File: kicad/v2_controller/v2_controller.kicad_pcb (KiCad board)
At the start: 2 copper layers, 100 x 116 mm, 131 parts, among them J1 Conn_02x10_Odd_Even, J2 Conn_02x10_Odd_Even, J3 USB_C_Receptacle_USB2.0, J4 USB_C_Receptacle_USB2.0, J5 Conn_02x04_Odd_Even, Q1 S8050, Q2 S8050, SW18 Boot, SW19 Reset, U1 ESP32-S3-WROOM-1-N16R8, U2 SSD1306_I2C, U3 74AHCT1G125, U4 AMS1117-3.3, U5 USBLC6-2P6, U6 USBLC6-2P6, U7 CP2102N-Axx-xQFN24

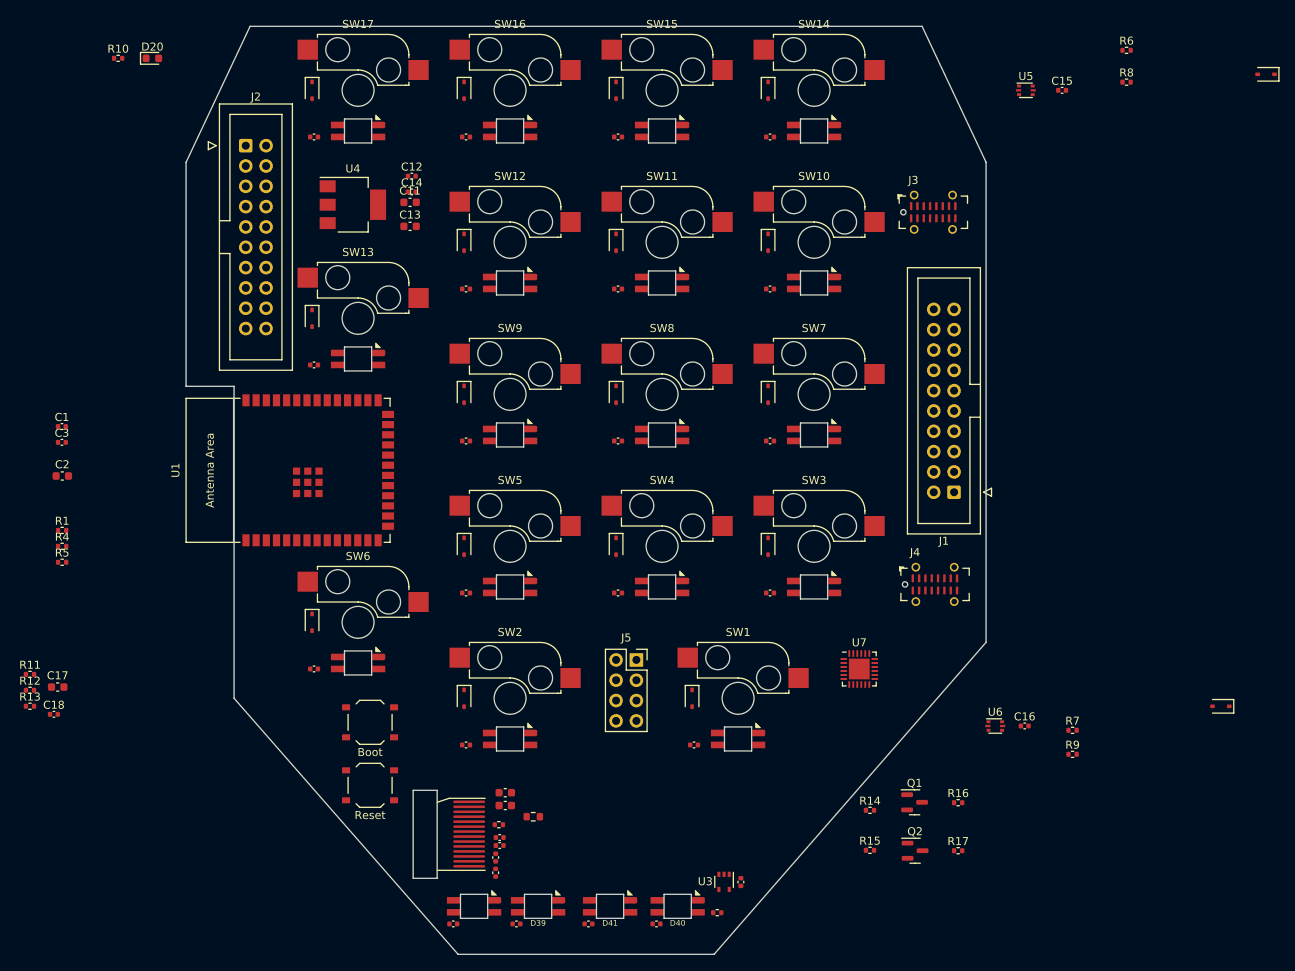
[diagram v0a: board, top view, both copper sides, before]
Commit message: [kicad] finish initial component placement
This will probably need to be tweaked further once I begin routing,
but is a start for now.
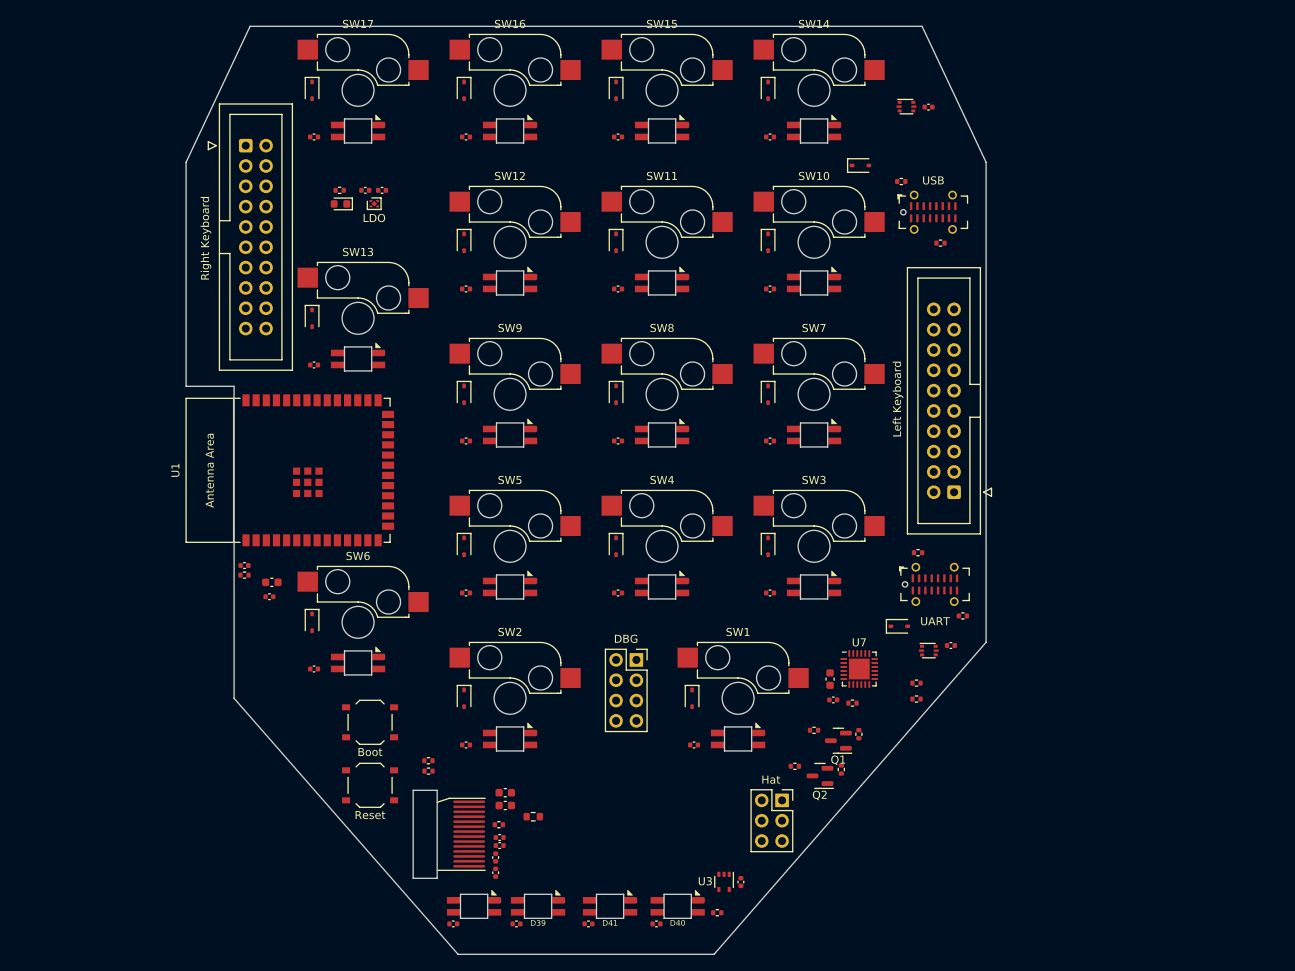
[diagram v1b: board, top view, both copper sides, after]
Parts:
- removed C13: 10uF, Capacitor_SMD:C_0603_1608Metric
- removed C14: 100nF, Capacitor_SMD:C_0402_1005Metric
- added J6: Conn_02x03_Odd_Even, Connector_PinSocket_2.54mm:PinSocket_2x03_P2.54mm_Vertical, F.Cu at (114.5, 136.8)
- C11: value 10uF -> 1uF; footprint Capacitor_SMD:C_0603_1608Metric -> Capacitor_SMD:C_0402_1005Metric
- C12: value 100nF -> 1uF
- U4: value AMS1117-3.3 -> NCP167BMX330TBG; footprint Package_TO_SOT_SMD:SOT-223-3_TabPin2 -> Package_DFN_QFN:OnSemi_XDFN4-1EP_1.0x1.0mm_EP0.52x0.52mm
- moved R13 110.8 mm to (131.3, 122.1)
- moved R14 110.8 mm to (131.3, 124.1)
- moved R15 102.8 mm to (123.3, 124.6), turned to 180 degrees
- moved C18 97.4 mm to (120.9, 124.2)
- moved C17 96.6 mm to (120.5, 121.6), turned to -90 degrees
- moved R2 53.0 mm to (70.3, 131.8)
- moved R3 52.7 mm to (70.3, 133.1)
- moved D18 52.0 mm to (124.3, 57.4), turned to 0 degrees
- moved D19 41.4 mm to (129.2, 115.0), turned to 0 degrees
- moved R8 32.6 mm to (129.4, 59.4)
- moved C3 32.3 mm to (50.4, 111.3)
- moved R12 32.2 mm to (59.2, 60.5)
- moved R9 30.8 mm to (134.3, 67.1)
- moved D20 29.7 mm to (59.3, 62.2), turned to 180 degrees
- moved R10 29.4 mm to (131.5, 105.8), turned to 180 degrees
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- renumbered J3 to J1, J4 to J2, J1 to J3, J2 to J4, R7 to R10, R9 to R11, R10 to R12, R11 to R13, R12 to R14, R13 to R15, R18 to R16, R2 to R17, R3 to R18, R4 to R2, R5 to R3, R14 to R4, R15 to R5, R16 to R6, R17 to R7, R6 to R8, R8 to R9
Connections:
- net /USB/USB1_VBUS renamed /USB/USB_VBUS
- C12 pad 1: +5V -> +3.3V
- C16 pad 1: /USB/USB2_VBUS -> /USB/UART_USB_VBUS
- D19 pad 2: /USB/USB2_VBUS -> /USB/UART_USB_VBUS
- J2 pad A4: /USB/USB2_VBUS -> /USB/UART_USB_VBUS
- J2 pad A9: /USB/USB2_VBUS -> /USB/UART_USB_VBUS
- J2 pad B4: /USB/USB2_VBUS -> /USB/UART_USB_VBUS
- J2 pad B9: /USB/USB2_VBUS -> /USB/UART_USB_VBUS
- R13 pad 1: +5V -> /USB/UART_USB_VBUS
- U1 pad 25: unconnected-(U1-GPIO48/SPICLK_N-Pad25) -> /ESP32/COL10
- U4 pad 1: GND -> +3.3V
- U4 pad 2: +3.3V -> GND
- U6 pad 5: /USB/USB2_VBUS -> /USB/UART_USB_VBUS

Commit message: [kicad] move the main USB receptacle closer to the ESP32
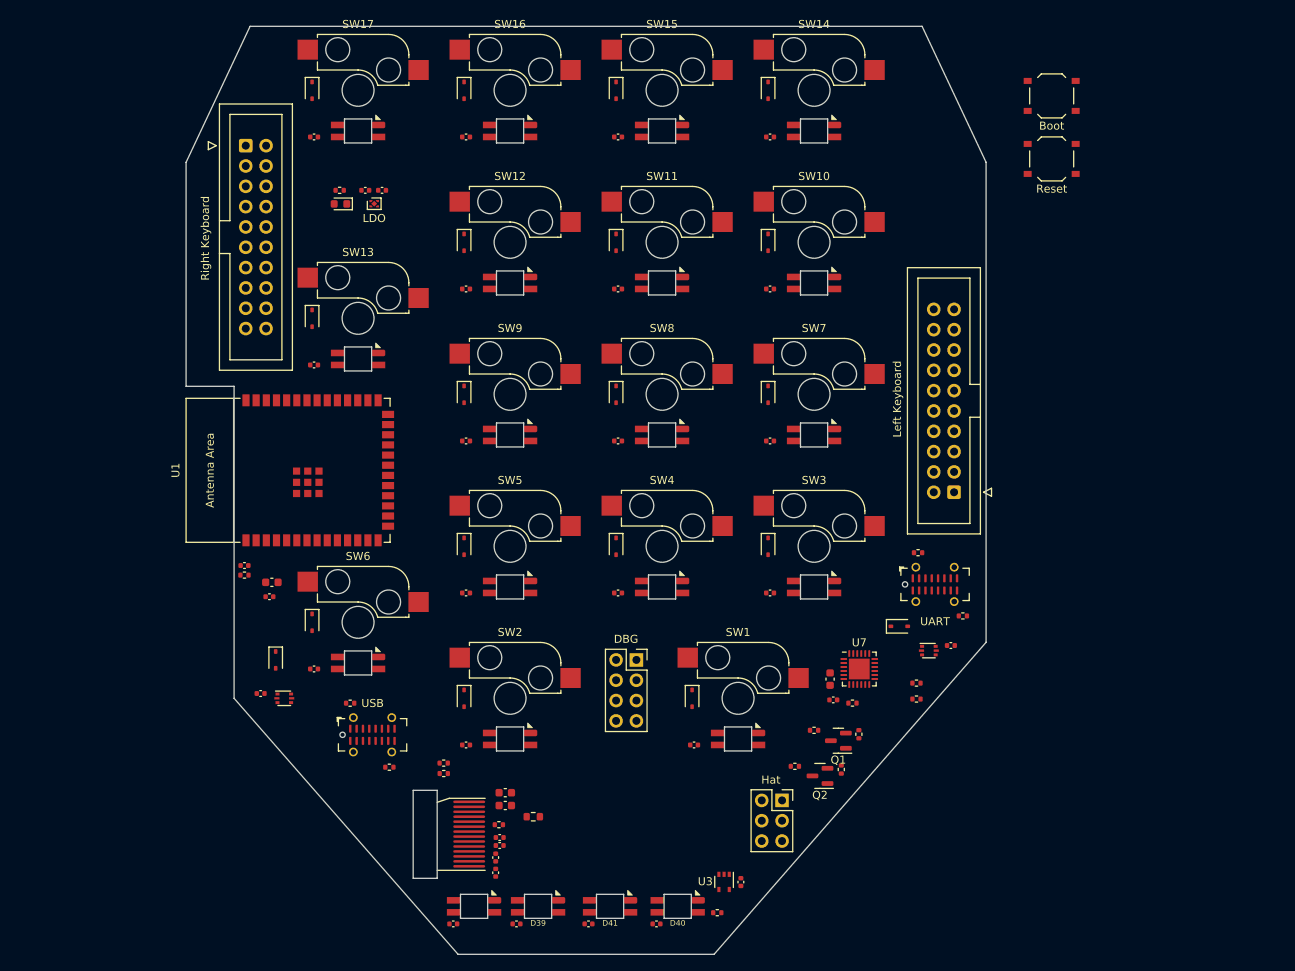
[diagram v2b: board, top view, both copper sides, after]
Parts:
- moved SW18 115.7 mm to (148.2, 48.7)
- moved SW19 115.7 mm to (148.2, 56.6)
- moved C15 111.1 mm to (49.3, 123.4)
- moved U5 107.3 mm to (52.3, 124.0)
- moved J1 95.8 mm to (63.3, 128.6)
- moved D18 95.7 mm to (51.2, 119.2), turned to -90 degrees
- moved R9 95.1 mm to (65.4, 132.6)
- moved R8 94.9 mm to (60.5, 124.6), turned to 180 degrees
- moved R3 1.93 mm to (72.2, 133.4)
- moved R2 1.93 mm to (72.2, 132.1)
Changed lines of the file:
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@@
   )
   (footprint "Resistor_SMD:R_0402_1005Metric" (layer "F.Cu")
-    (at 129.4 59.4)
+    (at 60.51 124.61 180)
     (descr "Resistor SMD 0402 (1005 Metric), square (rectangular) end terminal, IPC_7351 nominal, (Body size source: IPC-SM-782 page 72, https://www.pcb-3d.com/wordpress/wp-content/uploads/ipc-sm-782a_amendment_1_and_2.pdf), generated with kicad-footprint-generator")
     (tags "resistor")
@@
     (fp_line (start 0.525 0.27) (end -0.525 0.27)
       (stroke (width 0.1) (type solid)) (layer "F.Fab"))
-    (pad "1" smd roundrect (at -0.51 0) (size 0.54 0.64) (layers "F.Cu" "F.Paste" "F.Mask") (roundrect_rratio 0.25)
+    (pad "1" smd roundrect (at -0.51 0 180) (size 0.54 0.64) (layers "F.Cu" "F.Paste" "F.Mask") (roundrect_rratio 0.25)
       (net 67 "Net-(J1-CC1)") (pintype "passive"))
-    (pad "2" smd roundrect (at 0.51 0) (size 0.54 0.64) (layers "F.Cu" "F.Paste" "F.Mask") (roundrect_rratio 0.25)
+    (pad "2" smd roundrect (at 0.51 0 180) (size 0.54 0.64) (layers "F.Cu" "F.Paste" "F.Mask") (roundrect_rratio 0.25)
       (net 1 "GND") (pintype "passive"))
     (model "${KICAD6_3DMODEL_DIR}/Resistor_SMD.3dshapes/R_0402_1005Metric.wrl"
@@
   )
   (footprint "Connector_USB:USB_C_Receptacle_G-Switch_GT-USB-7051x" (layer "F.Cu")
-    (at 133.41 63.24)
+    (at 63.31 128.56)
     (descr "USB Type C, vertical, SMT, https://datasheet.lcsc.com/lcsc/2108072030_G-Switch-GT-USB-7051A_C2843970.pdf")
     (tags "USB C Type-C Receptacle SMD GT-USB-7051A GT-USB-7051B")
@@
       (polygon
         (pts
-          (xy 134.21 61.44)
-          (xy 132.61 61.44)
-          (xy 132.61 60.74)
-          (xy 134.21 60.74)
+          (xy 64.11 126.76)
+          (xy 62.51 126.76)
+          (xy 62.51 126.06)
+          (xy 64.11 126.06)
         )
       )
@@
       (polygon
         (pts
-          (xy 134.21 65.74)
-          (xy 132.61 65.74)
-          (xy 132.61 65.04)
-          (xy 134.21 65.04)
+          (xy 64.11 131.06)
+          (xy 62.51 131.06)
+          (xy 62.51 130.36)
+          (xy 64.11 130.36)
         )
       )
@@
   )
   (footprint "Resistor_SMD:R_0402_1005Metric" (layer "F.Cu")
-    (at 70.3 133.1)
+    (at 72.21 133.4)
     (descr "Resistor SMD 0402 (1005 Metric), square (rectangular) end terminal, IPC_7351 nominal, (Body size source: IPC-SM-782 page 72, https://www.pcb-3d.com/wordpress/wp-content/uploads/ipc-sm-782a_amendment_1_and_2.pdf), generated with kicad-footprint-generator")
     (tags "resistor")
@@
   )
   (footprint "Resistor_SMD:R_0402_1005Metric" (layer "F.Cu")
-    (at 134.3 67.1)
+    (at 65.41 132.61)
     (descr "Resistor SMD 0402 (1005 Metric), square (rectangular) end terminal, IPC_7351 nominal, (Body size source: IPC-SM-782 page 72, https://www.pcb-3d.com/wordpress/wp-content/uploads/ipc-sm-782a_amendment_1_and_2.pdf), generated with kicad-footprint-generator")
     (tags "resistor")
@@
   )
   (footprint "Resistor_SMD:R_0402_1005Metric" (layer "F.Cu")
-    (at 70.29 131.8)
+    (at 72.2 132.1)
     (descr "Resistor SMD 0402 (1005 Metric), square (rectangular) end terminal, IPC_7351 nominal, (Body size source: IPC-SM-782 page 72, https://www.pcb-3d.com/wordpress/wp-content/uploads/ipc-sm-782a_amendment_1_and_2.pdf), generated with kicad-footprint-generator")
     (tags "resistor")
@@
   )
   (footprint "Capacitor_SMD:C_0402_1005Metric" (layer "F.Cu")
-    (at 132.8 50.1)
+    (at 49.32 123.4)
     (descr "Capacitor SMD 0402 (1005 Metric), square (rectangular) end terminal, IPC_7351 nominal, (Body size source: IPC-SM-782 page 76, https://www.pcb-3d.com/wordpress/wp-content/uploads/ipc-sm-782a_amendment_1_and_2.pdf), generated with kicad-footprint-generator")
     (tags "capacitor")
@@
   )
   (footprint "Button_Switch_SMD:SW_Push_1P1T_XKB_TS-1187A" (layer "F.Cu")
-    (at 63 134.875)
+    (at 148.2 56.575)
     (descr "SMD Tactile Switch, http://www.helloxkb.com/public/images/pdf/TS-1187A-X-X-X.pdf")
     (tags "SPST Tactile Switch")
@@
   )
   (footprint "Button_Switch_SMD:SW_Push_1P1T_XKB_TS-1187A" (layer "F.Cu")
-    (at 63 127)
+    (at 148.2 48.7)
     (descr "SMD Tactile Switch, http://www.helloxkb.com/public/images/pdf/TS-1187A-X-X-X.pdf")
     (tags "SPST Tactile Switch")
@@
   )
   (footprint "Package_TO_SOT_SMD:SOT-666" (layer "F.Cu")
-    (at 130.05 50.0375)
+    (at 52.275 124)
     (descr "SOT666")
     (tags "SOT-666")
@@
   )
   (footprint "Diode_SMD:D_SOD-323" (layer "F.Cu")
-    (at 124.3 57.4)
+    (at 51.2 119.2 -90)
     (descr "SOD-323")
     (tags "SOD-323")
@@
     (property "ki_keywords" "diode Schottky")
     (attr smd)
-    (fp_text reference "D18" (at 0 -1.85) (layer "F.SilkS") hide
+    (fp_text reference "D18" (at 0 -1.85 90) (layer "F.SilkS") hide
         (effects (font (size 1 1) (thickness 0.15)))
     )
-    (fp_text value "1N5819WS" (at 0.1 1.9) (layer "F.Fab")
+    (fp_text value "1N5819WS" (at 0.1 1.9 90) (layer "F.Fab")
         (effects (font (size 1 1) (thickness 0.15)))
     )
-    (fp_text user "${REFERENCE}" (at 0 -1.85) (layer "F.Fab")
+    (fp_text user "${REFERENCE}" (at 0 -1.85 90) (layer "F.Fab")
         (effects (font (size 1 1) (thickness 0.15)))
     )
@@
     (fp_line (start 0.9 0.7) (end -0.9 0.7)
       (stroke (width 0.1) (type solid)) (layer "F.Fab"))
-    (pad "1" smd roundrect (at -1.05 0) (size 0.6 0.45) (layers "F.Cu" "F.Paste" "F.Mask") (roundrect_rratio 0.25)
+    (pad "1" smd roundrect (at -1.05 0 270) (size 0.6 0.45) (layers "F.Cu" "F.Paste" "F.Mask") (roundrect_rratio 0.25)
       (net 9 "+5V") (pinfunction "K") (pintype "passive"))
-    (pad "2" smd roundrect (at 1.05 0) (size 0.6 0.45) (layers "F.Cu" "F.Paste" "F.Mask") (roundrect_rratio 0.25)
+    (pad "2" smd roundrect (at 1.05 0 270) (size 0.6 0.45) (layers "F.Cu" "F.Paste" "F.Mask") (roundrect_rratio 0.25)
       (net 129 "/USB/USB_VBUS") (pinfunction "A") (pintype "passive"))
     (model "${KICAD6_3DMODEL_DIR}/Diode_SMD.3dshapes/D_SOD-323.wrl"

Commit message: [kicad] tweak the pcb layout with a slightly larger board
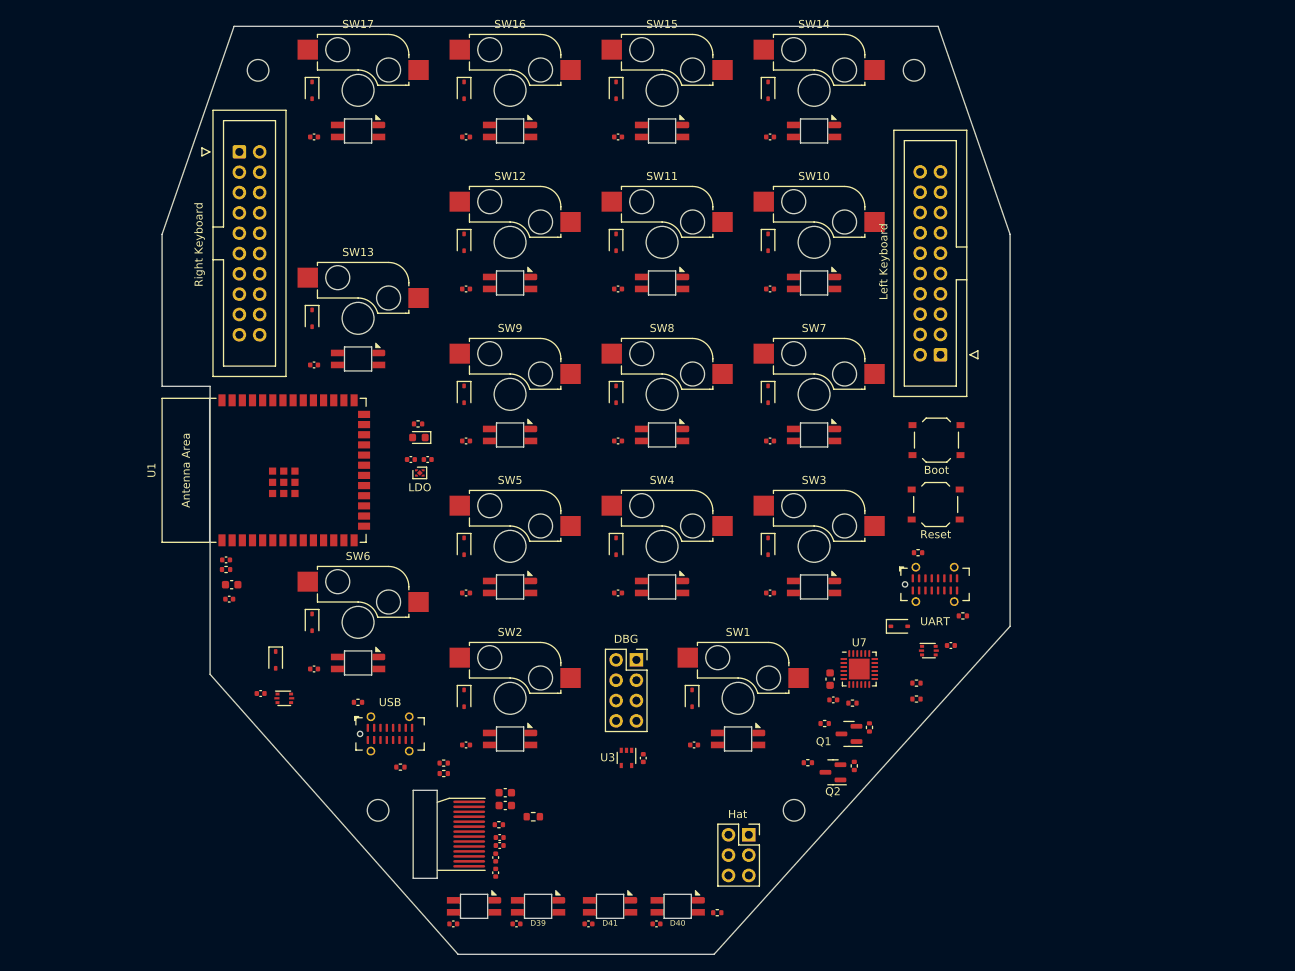
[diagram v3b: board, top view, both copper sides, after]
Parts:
- added REF**: MountingHole_2.7mm_M2.5, MountingHole:MountingHole_2.7mm_M2.5, F.Cu at (116.0, 138.0)
- added REF**: MountingHole_2.7mm_M2.5, MountingHole:MountingHole_2.7mm_M2.5, F.Cu at (64.0, 138.0)
- added REF**: MountingHole_2.7mm_M2.5, MountingHole:MountingHole_2.7mm_M2.5, F.Cu at (131.0, 45.5)
- added REF**: MountingHole_2.7mm_M2.5, MountingHole:MountingHole_2.7mm_M2.5, F.Cu at (49.0, 45.5)
- moved SW19 45.6 mm to (133.7, 99.8)
- moved SW18 45.4 mm to (133.8, 91.7)
- moved C11 34.1 mm to (70.2, 94.2)
- moved C12 34.1 mm to (68.1, 94.2)
- moved U4 34.1 mm to (69.2, 95.8)
- moved D20 30.8 mm to (69.1, 91.4)
- moved R12 30.8 mm to (69.0, 89.7)
- moved U3 19.7 mm to (95.0, 131.4)
- moved C10 19.7 mm to (97.2, 131.5)
- moved J3 17.3 mm to (134.3, 81.1)
- moved J6 5.98 mm to (110.3, 141.1)
- moved C2 5.03 mm to (45.7, 109.8)
- moved C3 5.03 mm to (45.4, 111.6)
- moved U1 3.00 mm to (52.8, 95.5)
- moved C1 2.40 mm to (45.0, 106.7)
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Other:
- board size 100 x 116 mm -> 106 x 116 mm

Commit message: [kicad] more minor tweaks
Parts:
- removed the REF** at (116.0, 138.0)
- removed the REF** at (64.0, 138.0)
- removed the REF** at (131.0, 45.5)
- removed the REF** at (49.0, 45.5)
- added REF**: MountingHole_2.7mm_M2.5, MountingHole:MountingHole_2.7mm_M2.5, F.Cu at (131.5, 45.5)
- added REF**: MountingHole_2.7mm_M2.5, MountingHole:MountingHole_2.7mm_M2.5, F.Cu at (116.0, 139.0)
- added REF**: MountingHole_2.7mm_M2.5, MountingHole:MountingHole_2.7mm_M2.5, F.Cu at (64.0, 139.0)
- added REF**: MountingHole_2.7mm_M2.5, MountingHole:MountingHole_2.7mm_M2.5, F.Cu at (48.5, 45.5)
- moved R9 73.9 mm to (69.3, 58.7), turned to 180 degrees
- moved J1 66.2 mm to (61.3, 62.4), turned to 180 degrees
- moved R8 65.0 mm to (69.5, 60.0)
- moved U5 63.2 mm to (71.1, 63.7), turned to -90 degrees
- moved C15 61.3 mm to (68.7, 65.2), turned to 90 degrees
- moved D18 55.3 mm to (71.2, 67.7), turned to 90 degrees
- moved R16 35.0 mm to (71.5, 147.9)
- moved C37 23.8 mm to (104.8, 148.0)
- moved C36 23.7 mm to (96.8, 148.0)
- moved D38 23.5 mm to (78.0, 150.0), turned to 180 degrees
- moved C38 18.5 mm to (80.8, 148.0)
- moved D40 18.0 mm to (94.0, 150.0), turned to 180 degrees
- moved D41 18.0 mm to (102.0, 150.0), turned to 180 degrees
- moved D39 7.00 mm to (86.0, 150.0), turned to 180 degrees
- moved C39 4.47 mm to (88.8, 148.0)
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- renumbered D40 to D38, D41 to D39, D38 to D40, D39 to D41
